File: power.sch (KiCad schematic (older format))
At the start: 42 parts, among them CN400 POWER_CONN, U108 74LS74A, U607 74LS08

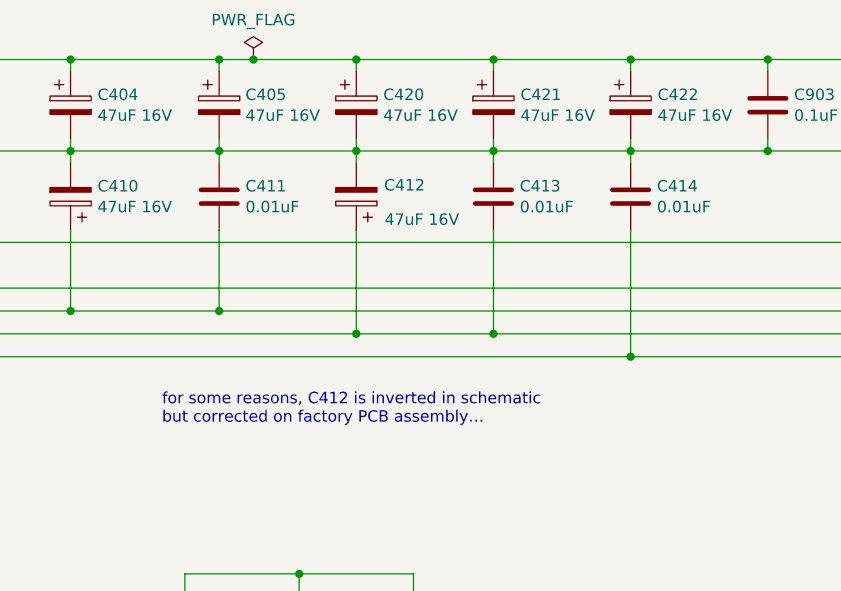
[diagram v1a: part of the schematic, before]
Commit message: Switch footprints for suitable modern replacements
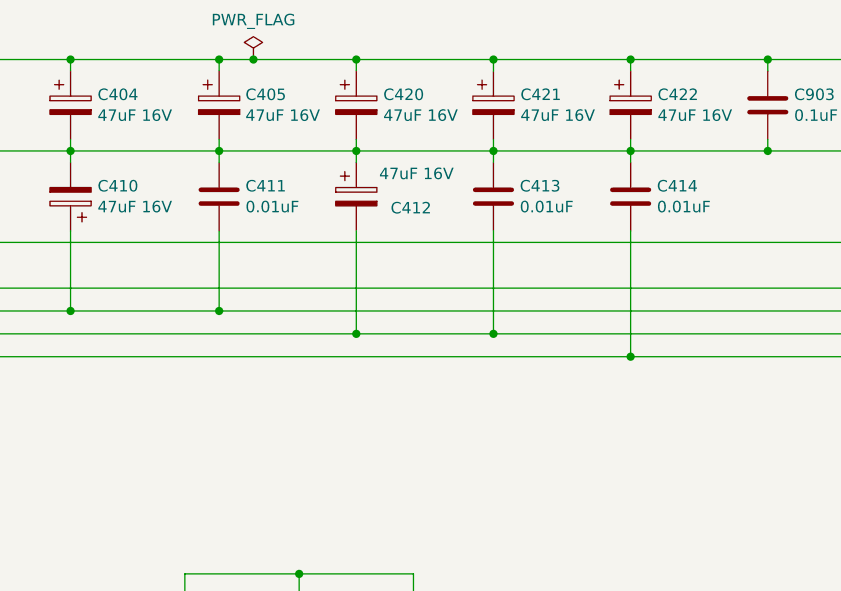
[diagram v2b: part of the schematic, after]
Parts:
- C401, C407, C409, C411, C413, C414, C903, C906, C910: footprint Capacitor_THT:C_Rect_L11.5mm_W2.0mm_P10.00mm_MKT -> Capacitor_THT:C_Rect_L11.5mm_W2.6mm_P10.00mm_MKT
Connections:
- net -5V: now also C412.2; no longer C412.1
- net GND: now also C412.1; no longer C412.2
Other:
- note removed: "for some reasons, C412 is inverted in schematic\nbut corrected on factory PCB assembly…"
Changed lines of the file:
@@
 F 0 "C401" H 2165 1746 50  0000 L CNN
 F 1 "0.01uF" H 2165 1655 50  0000 L CNN
-F 2 "Capacitor_THT:C_Rect_L11.5mm_W2.0mm_P10.00mm_MKT" H 2088 1550 50  0001 C CNN
+F 2 "Capacitor_THT:C_Rect_L11.5mm_W2.6mm_P10.00mm_MKT" H 2088 1550 50  0001 C CNN
 F 3 "~" H 2050 1700 50  0001 C CNN
 	1    2050 1700
@@
 F 0 "C407" H 2165 2146 50  0000 L CNN
 F 1 "0.01uF" H 2165 2055 50  0000 L CNN
-F 2 "Capacitor_THT:C_Rect_L11.5mm_W2.0mm_P10.00mm_MKT" H 2088 1950 50  0001 C CNN
+F 2 "Capacitor_THT:C_Rect_L11.5mm_W2.6mm_P10.00mm_MKT" H 2088 1950 50  0001 C CNN
 F 3 "~" H 2050 2100 50  0001 C CNN
 	1    2050 2100
-	1    0    0    -1
-$EndComp
-$Comp
-L Device:CP C408
-U 1 1 5DDDE124
-P 3050 2100
-F 0 "C408" H 3168 2146 50  0000 L CNN
-F 1 "47uF 16V" H 3168 2055 50  0000 L CNN
-F 2 "Capacitor_THT:CP_Radial_D8.0mm_P5.00mm" H 3088 1950 50  0001 C CNN
-F 3 "~" H 3050 2100 50  0001 C CNN
-	1    3050 2100
 	1    0    0    -1
 $EndComp
@@
 F 0 "C409" H 3815 2146 50  0000 L CNN
 F 1 "0.01uF" H 3815 2055 50  0000 L CNN
-F 2 "Capacitor_THT:C_Rect_L11.5mm_W2.0mm_P10.00mm_MKT" H 3738 1950 50  0001 C CNN
+F 2 "Capacitor_THT:C_Rect_L11.5mm_W2.6mm_P10.00mm_MKT" H 3738 1950 50  0001 C CNN
 F 3 "~" H 3700 2100 50  0001 C CNN
 	1    3700 2100
@@
 F 0 "C411" H 5265 2146 50  0000 L CNN
 F 1 "0.01uF" H 5265 2055 50  0000 L CNN
-F 2 "Capacitor_THT:C_Rect_L11.5mm_W2.0mm_P10.00mm_MKT" H 5188 1950 50  0001 C CNN
+F 2 "Capacitor_THT:C_Rect_L11.5mm_W2.6mm_P10.00mm_MKT" H 5188 1950 50  0001 C CNN
 F 3 "~" H 5150 2100 50  0001 C CNN
 	1    5150 2100
@@
 U 1 1 5DDDF78A
 P 5750 2100
-F 0 "C412" H 5450 2050 50  0000 L CNN
-F 1 "47uF 16V" H 5300 2200 50  0000 L CNN
+F 0 "C412" H 5900 2050 50  0000 L CNN
+F 1 "47uF 16V" H 5850 2200 50  0000 L CNN
 F 2 "Capacitor_THT:CP_Radial_D8.0mm_P5.00mm" H 5788 1950 50  0001 C CNN
 F 3 "~" H 5750 2100 50  0001 C CNN
 	1    5750 2100
-	-1   0    0    1
+	1    0    0    -1
 $EndComp
 $Comp
@@
 F 0 "C413" H 6465 2146 50  0000 L CNN
 F 1 "0.01uF" H 6465 2055 50  0000 L CNN
-F 2 "Capacitor_THT:C_Rect_L11.5mm_W2.0mm_P10.00mm_MKT" H 6388 1950 50  0001 C CNN
+F 2 "Capacitor_THT:C_Rect_L11.5mm_W2.6mm_P10.00mm_MKT" H 6388 1950 50  0001 C CNN
 F 3 "~" H 6350 2100 50  0001 C CNN
 	1    6350 2100
@@
 F 0 "C414" H 7065 2146 50  0000 L CNN
 F 1 "0.01uF" H 7065 2055 50  0000 L CNN
-F 2 "Capacitor_THT:C_Rect_L11.5mm_W2.0mm_P10.00mm_MKT" H 6988 1950 50  0001 C CNN
+F 2 "Capacitor_THT:C_Rect_L11.5mm_W2.6mm_P10.00mm_MKT" H 6988 1950 50  0001 C CNN
 F 3 "~" H 6950 2100 50  0001 C CNN
 	1    6950 2100
@@
 F 0 "C903" H 7665 1746 50  0000 L CNN
 F 1 "0.1uF" H 7665 1655 50  0000 L CNN
-F 2 "Capacitor_THT:C_Rect_L11.5mm_W2.0mm_P10.00mm_MKT" H 7588 1550 50  0001 C CNN
+F 2 "Capacitor_THT:C_Rect_L11.5mm_W2.6mm_P10.00mm_MKT" H 7588 1550 50  0001 C CNN
 F 3 "~" H 7550 1700 50  0001 C CNN
 	1    7550 1700
@@
 F 0 "C906" H 8115 1746 50  0000 L CNN
 F 1 "0.1uF" H 8115 1655 50  0000 L CNN
-F 2 "Capacitor_THT:C_Rect_L11.5mm_W2.0mm_P10.00mm_MKT" H 8038 1550 50  0001 C CNN
+F 2 "Capacitor_THT:C_Rect_L11.5mm_W2.6mm_P10.00mm_MKT" H 8038 1550 50  0001 C CNN
 F 3 "~" H 8000 1700 50  0001 C CNN
 	1    8000 1700
@@
 F 0 "C910" H 8565 1746 50  0000 L CNN
 F 1 "0.1uF" H 8565 1655 50  0000 L CNN
-F 2 "Capacitor_THT:C_Rect_L11.5mm_W2.0mm_P10.00mm_MKT" H 8488 1550 50  0001 C CNN
+F 2 "Capacitor_THT:C_Rect_L11.5mm_W2.6mm_P10.00mm_MKT" H 8488 1550 50  0001 C CNN
 F 3 "~" H 8450 1700 50  0001 C CNN
 	1    8450 1700
@@
 Wire Wire Line
 	6000 4350 6000 4300
-Text Notes 4900 3100 0    50   ~ 0
-for some reasons, C412 is inverted in schematic\nbut corrected on factory PCB assembly…
+$Comp
+L Device:CP C408
+U 1 1 5DDDE124
+P 3050 2100
+F 0 "C408" H 3168 2146 50  0000 L CNN
+F 1 "47uF 16V" H 3168 2055 50  0000 L CNN
+F 2 "Capacitor_THT:CP_Radial_D8.0mm_P5.00mm" H 3088 1950 50  0001 C CNN
+F 3 "~" H 3050 2100 50  0001 C CNN
+	1    3050 2100
+	1    0    0    -1
+$EndComp
 $EndSCHEMATC

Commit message: Some footprints updates; Add all Mouser references
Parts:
- C400: RefOrder (none) -> 667-ECA-1CM221B
- C401, C407, C409, C411, C413, C414: RefOrder (none) -> 581-SA105C103K
- C402, C403, C404, C405, C406, C408, C410, C412, C420, C421, C422: RefOrder (none) -> 667-ECA-1CM470B
- C903, C906, C910: RefOrder (none) -> 581-SA105C104KARC
- D400, D401: RefOrder (none) -> 750-1N4001-G
- H1, H10, H11, H12, H13, H14, H2, H3, H4, H5, H6, H7, H8, H9: DoNotPopulate (none) -> yes
- U108: RefOrder (none) -> 595-SN74LS74AN
- U607: RefOrder (none) -> 595-SN74LS08N
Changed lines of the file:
@@
 F 2 "Capacitor_THT:CP_Radial_D8.0mm_P5.00mm" H 1438 1550 50  0001 C CNN
 F 3 "~" H 1400 1700 50  0001 C CNN
+F 4 "667-ECA-1CM221B" H 1400 1700 50  0001 C CNN "RefOrder"
 	1    1400 1700
 	1    0    0    -1
@@
 F 2 "Capacitor_THT:C_Rect_L11.5mm_W2.6mm_P10.00mm_MKT" H 2088 1550 50  0001 C CNN
 F 3 "~" H 2050 1700 50  0001 C CNN
+F 4 "581-SA105C103K" H 2050 1700 50  0001 C CNN "RefOrder"
 	1    2050 1700
 	1    0    0    -1
@@
 F 2 "Capacitor_THT:CP_Radial_D8.0mm_P5.00mm" H 3088 1550 50  0001 C CNN
 F 3 "~" H 3050 1700 50  0001 C CNN
+F 4 "667-ECA-1CM470B" H 3050 1700 50  0001 C CNN "RefOrder"
 	1    3050 1700
 	1    0    0    -1
@@
 F 2 "Capacitor_THT:CP_Radial_D8.0mm_P5.00mm" H 3738 1550 50  0001 C CNN
 F 3 "~" H 3700 1700 50  0001 C CNN
+F 4 "667-ECA-1CM470B" H 3700 1700 50  0001 C CNN "RefOrder"
 	1    3700 1700
 	1    0    0    -1
@@
 F 2 "Capacitor_THT:CP_Radial_D8.0mm_P5.00mm" H 4538 1550 50  0001 C CNN
 F 3 "~" H 4500 1700 50  0001 C CNN
+F 4 "667-ECA-1CM470B" H 4500 1700 50  0001 C CNN "RefOrder"
 	1    4500 1700
 	1    0    0    -1
@@
 F 2 "Capacitor_THT:CP_Radial_D8.0mm_P5.00mm" H 5188 1550 50  0001 C CNN
 F 3 "~" H 5150 1700 50  0001 C CNN
+F 4 "667-ECA-1CM470B" H 5150 1700 50  0001 C CNN "RefOrder"
 	1    5150 1700
 	1    0    0    -1
@@
 F 2 "Capacitor_THT:CP_Radial_D8.0mm_P5.00mm" H 1438 1950 50  0001 C CNN
 F 3 "~" H 1400 2100 50  0001 C CNN
+F 4 "667-ECA-1CM470B" H 1400 2100 50  0001 C CNN "RefOrder"
 	1    1400 2100
 	-1   0    0    1
@@
 F 2 "Capacitor_THT:C_Rect_L11.5mm_W2.6mm_P10.00mm_MKT" H 2088 1950 50  0001 C CNN
 F 3 "~" H 2050 2100 50  0001 C CNN
+F 4 "581-SA105C103K" H 2050 2100 50  0001 C CNN "RefOrder"
 	1    2050 2100
 	1    0    0    -1
@@
 F 2 "Capacitor_THT:C_Rect_L11.5mm_W2.6mm_P10.00mm_MKT" H 3738 1950 50  0001 C CNN
 F 3 "~" H 3700 2100 50  0001 C CNN
+F 4 "581-SA105C103K" H 3700 2100 50  0001 C CNN "RefOrder"
 	1    3700 2100
 	1    0    0    -1
@@
 F 2 "Capacitor_THT:CP_Radial_D8.0mm_P5.00mm" H 4538 1950 50  0001 C CNN
 F 3 "~" H 4500 2100 50  0001 C CNN
+F 4 "667-ECA-1CM470B" H 4500 2100 50  0001 C CNN "RefOrder"
 	1    4500 2100
 	-1   0    0    1
@@
 F 2 "Capacitor_THT:C_Rect_L11.5mm_W2.6mm_P10.00mm_MKT" H 5188 1950 50  0001 C CNN
 F 3 "~" H 5150 2100 50  0001 C CNN
+F 4 "581-SA105C103K" H 5150 2100 50  0001 C CNN "RefOrder"
 	1    5150 2100
 	1    0    0    -1
@@
 F 2 "Capacitor_THT:CP_Radial_D8.0mm_P5.00mm" H 5788 1950 50  0001 C CNN
 F 3 "~" H 5750 2100 50  0001 C CNN
+F 4 "667-ECA-1CM470B" H 5750 2100 50  0001 C CNN "RefOrder"
 	1    5750 2100
 	1    0    0    -1
@@
 F 2 "Capacitor_THT:C_Rect_L11.5mm_W2.6mm_P10.00mm_MKT" H 6388 1950 50  0001 C CNN
 F 3 "~" H 6350 2100 50  0001 C CNN
+F 4 "581-SA105C103K" H 6350 2100 50  0001 C CNN "RefOrder"
 	1    6350 2100
 	1    0    0    -1
@@
 F 2 "Capacitor_THT:C_Rect_L11.5mm_W2.6mm_P10.00mm_MKT" H 6988 1950 50  0001 C CNN
 F 3 "~" H 6950 2100 50  0001 C CNN
+F 4 "581-SA105C103K" H 6950 2100 50  0001 C CNN "RefOrder"
 	1    6950 2100
 	1    0    0    -1
@@
 F 2 "Diode_THT:D_DO-41_SOD81_P10.16mm_Horizontal" H 9300 1975 50  0001 C CNN
 F 3 "http://www.vishay.com/docs/88503/1n4001.pdf" H 9300 2150 50  0001 C CNN
+F 4 "750-1N4001-G" H 9300 2150 50  0001 C CNN "RefOrder"
 	1    9300 2150
 	0    1    1    0
@@
 F 2 "Diode_THT:D_DO-41_SOD81_P10.16mm_Horizontal" H 10100 1975 50  0001 C CNN
 F 3 "http://www.vishay.com/docs/88503/1n4001.pdf" H 10100 2150 50  0001 C CNN
+F 4 "750-1N4001-G" H 10100 2150 50  0001 C CNN "RefOrder"
 	1    10100 2150
 	0    -1   -1   0
@@
 F 2 "Package_DIP:DIP-14_W7.62mm_Socket" H 8450 4700 50  0001 C CNN
 F 3 "http://www.ti.com/lit/ds/symlink/sn74ls74a.pdf" H 8450 4700 50  0001 C CNN
+F 4 "595-SN74LS74AN" H 8450 4700 50  0001 C CNN "RefOrder"
 	1    8450 4700
 	1    0    0    -1
@@
 F 2 "Package_DIP:DIP-14_W7.62mm_Socket" H 8450 5650 50  0001 C CNN
 F 3 "http://www.ti.com/lit/gpn/sn74LS08" H 8450 5650 50  0001 C CNN
+F 4 "595-SN74LS08N" H 8450 5650 50  0001 C CNN "RefOrder"
 	3    8450 5650
 	1    0    0    -1
@@
 F 2 "Capacitor_THT:CP_Radial_D8.0mm_P5.00mm" H 5788 1550 50  0001 C CNN
 F 3 "~" H 5750 1700 50  0001 C CNN
+F 4 "667-ECA-1CM470B" H 5750 1700 50  0001 C CNN "RefOrder"
 	1    5750 1700
 	1    0    0    -1
@@
 F 2 "Capacitor_THT:CP_Radial_D8.0mm_P5.00mm" H 6388 1550 50  0001 C CNN
 F 3 "~" H 6350 1700 50  0001 C CNN
+F 4 "667-ECA-1CM470B" H 6350 1700 50  0001 C CNN "RefOrder"
 	1    6350 1700
 	1    0    0    -1
@@
 F 2 "Capacitor_THT:CP_Radial_D8.0mm_P5.00mm" H 6988 1550 50  0001 C CNN
 F 3 "~" H 6950 1700 50  0001 C CNN
+F 4 "667-ECA-1CM470B" H 6950 1700 50  0001 C CNN "RefOrder"
 	1    6950 1700
 	1    0    0    -1
@@
 F 2 "Capacitor_THT:C_Rect_L11.5mm_W2.6mm_P10.00mm_MKT" H 7588 1550 50  0001 C CNN
 F 3 "~" H 7550 1700 50  0001 C CNN
+F 4 "581-SA105C104KARC" H 7550 1700 50  0001 C CNN "RefOrder"
 	1    7550 1700
 	1    0    0    -1
@@
 F 2 "Capacitor_THT:C_Rect_L11.5mm_W2.6mm_P10.00mm_MKT" H 8038 1550 50  0001 C CNN
 F 3 "~" H 8000 1700 50  0001 C CNN
+F 4 "581-SA105C104KARC" H 8000 1700 50  0001 C CNN "RefOrder"
 	1    8000 1700
 	1    0    0    -1
@@
 F 2 "Capacitor_THT:C_Rect_L11.5mm_W2.6mm_P10.00mm_MKT" H 8488 1550 50  0001 C CNN
 F 3 "~" H 8450 1700 50  0001 C CNN
+F 4 "581-SA105C104KARC" H 8450 1700 50  0001 C CNN "RefOrder"
 	1    8450 1700
 	1    0    0    -1
@@
 F 2 "MountingHole:MountingHole_4mm_Pad_Via" H 1500 3900 50  0001 C CNN
 F 3 "~" H 1500 3900 50  0001 C CNN
+F 4 "yes" H 1500 3900 50  0001 C CNN "DoNotPopulate"
 	1    1500 3900
 	0    -1   -1   0
@@
 F 2 "MountingHole:MountingHole_4mm_Pad_Via" H 1500 4400 50  0001 C CNN
 F 3 "~" H 1500 4400 50  0001 C CNN
+F 4 "yes" H 1500 4400 50  0001 C CNN "DoNotPopulate"
 	1    1500 4400
 	0    -1   -1   0
@@
 F 2 "MountingHole:MountingHole_4mm_Pad_Via" H 1500 4900 50  0001 C CNN
 F 3 "~" H 1500 4900 50  0001 C CNN
+F 4 "yes" H 1500 4900 50  0001 C CNN "DoNotPopulate"
 	1    1500 4900
 	0    -1   -1   0
@@
 F 2 "MountingHole:MountingHole_4mm_Pad_Via" H 1500 5400 50  0001 C CNN
 F 3 "~" H 1500 5400 50  0001 C CNN
+F 4 "yes" H 1500 5400 50  0001 C CNN "DoNotPopulate"
 	1    1500 5400
 	0    -1   -1   0
@@
 F 2 "MountingHole:MountingHole_4mm_Pad_Via" H 1500 5900 50  0001 C CNN
 F 3 "~" H 1500 5900 50  0001 C CNN
+F 4 "yes" H 1500 5900 50  0001 C CNN "DoNotPopulate"
 	1    1500 5900
 	0    -1   -1   0
@@
 F 2 "MountingHole:MountingHole_4mm_Pad_Via" H 2500 3900 50  0001 C CNN
 F 3 "~" H 2500 3900 50  0001 C CNN
+F 4 "yes" H 2500 3900 50  0001 C CNN "DoNotPopulate"
 	1    2500 3900
 	0    1    1    0
@@
 F 2 "MountingHole:MountingHole_4mm_Pad_Via" H 2500 4400 50  0001 C CNN
 F 3 "~" H 2500 4400 50  0001 C CNN
+F 4 "yes" H 2500 4400 50  0001 C CNN "DoNotPopulate"
 	1    2500 4400
 	0    1    1    0
@@
 F 2 "MountingHole:MountingHole_4mm_Pad_Via" H 2500 4900 50  0001 C CNN
 F 3 "~" H 2500 4900 50  0001 C CNN
+F 4 "yes" H 2500 4900 50  0001 C CNN "DoNotPopulate"
 	1    2500 4900
 	0    1    1    0
@@
 F 2 "MountingHole:MountingHole_4mm_Pad_Via" H 2500 5900 50  0001 C CNN
 F 3 "~" H 2500 5900 50  0001 C CNN
+F 4 "yes" H 2500 5900 50  0001 C CNN "DoNotPopulate"
 	1    2500 5900
 	0    1    1    0
@@
 F 2 "MountingHole:MountingHole_4mm_Pad_Via" H 2500 5400 50  0001 C CNN
 F 3 "~" H 2500 5400 50  0001 C CNN
+F 4 "yes" H 2500 5400 50  0001 C CNN "DoNotPopulate"
 	1    2500 5400
 	0    1    1    0
@@
 F 2 "MountingHole:MountingHole_4mm_Pad_Via" H 2500 4150 50  0001 C CNN
 F 3 "~" H 2500 4150 50  0001 C CNN
+F 4 "yes" H 2500 4150 50  0001 C CNN "DoNotPopulate"
 	1    2500 4150
 	0    1    1    0
@@
 F 2 "MountingHole:MountingHole_4mm_Pad_Via" H 2500 4650 50  0001 C CNN
 F 3 "~" H 2500 4650 50  0001 C CNN
+F 4 "yes" H 2500 4650 50  0001 C CNN "DoNotPopulate"
 	1    2500 4650
 	0    1    1    0
@@
 F 2 "MountingHole:MountingHole_4mm_Pad_Via" H 2500 5150 50  0001 C CNN
 F 3 "~" H 2500 5150 50  0001 C CNN
+F 4 "yes" H 2500 5150 50  0001 C CNN "DoNotPopulate"
 	1    2500 5150
 	0    1    1    0
@@
 F 2 "MountingHole:MountingHole_4mm_Pad_Via" H 2500 5650 50  0001 C CNN
 F 3 "~" H 2500 5650 50  0001 C CNN
+F 4 "yes" H 2500 5650 50  0001 C CNN "DoNotPopulate"
 	1    2500 5650
 	0    1    1    0
@@
 F 2 "Capacitor_THT:CP_Radial_D8.0mm_P5.00mm" H 3088 1950 50  0001 C CNN
 F 3 "~" H 3050 2100 50  0001 C CNN
+F 4 "667-ECA-1CM470B" H 3050 2100 50  0001 C CNN "RefOrder"
 	1    3050 2100
 	1    0    0    -1

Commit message: Got the components, reduce some footprints
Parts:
- C400: footprint Capacitor_THT:CP_Radial_D8.0mm_P5.00mm -> Capacitor_THT:CP_Radial_Tantal_D6.0mm_P5.00mm
- C402, C403, C404, C405, C406, C408, C410, C412, C420, C421, C422: footprint Capacitor_THT:CP_Radial_D8.0mm_P5.00mm -> Capacitor_THT:CP_Radial_Tantal_D5.5mm_P5.00mm
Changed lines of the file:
@@
 F 0 "C400" H 1518 1746 50  0000 L CNN
 F 1 "220uF 16V" H 1518 1655 50  0000 L CNN
-F 2 "Capacitor_THT:CP_Radial_D8.0mm_P5.00mm" H 1438 1550 50  0001 C CNN
+F 2 "Capacitor_THT:CP_Radial_Tantal_D6.0mm_P5.00mm" H 1438 1550 50  0001 C CNN
 F 3 "~" H 1400 1700 50  0001 C CNN
 F 4 "667-ECA-1CM221B" H 1400 1700 50  0001 C CNN "RefOrder"
@@
 F 0 "C402" H 3168 1746 50  0000 L CNN
 F 1 "47uF 16V" H 3168 1655 50  0000 L CNN
-F 2 "Capacitor_THT:CP_Radial_D8.0mm_P5.00mm" H 3088 1550 50  0001 C CNN
+F 2 "Capacitor_THT:CP_Radial_Tantal_D5.5mm_P5.00mm" H 3088 1550 50  0001 C CNN
 F 3 "~" H 3050 1700 50  0001 C CNN
 F 4 "667-ECA-1CM470B" H 3050 1700 50  0001 C CNN "RefOrder"
@@
 F 0 "C403" H 3815 1746 50  0000 L CNN
 F 1 "47uF 16V" H 3815 1655 50  0000 L CNN
-F 2 "Capacitor_THT:CP_Radial_D8.0mm_P5.00mm" H 3738 1550 50  0001 C CNN
+F 2 "Capacitor_THT:CP_Radial_Tantal_D5.5mm_P5.00mm" H 3738 1550 50  0001 C CNN
 F 3 "~" H 3700 1700 50  0001 C CNN
 F 4 "667-ECA-1CM470B" H 3700 1700 50  0001 C CNN "RefOrder"
@@
 F 0 "C404" H 4618 1746 50  0000 L CNN
 F 1 "47uF 16V" H 4618 1655 50  0000 L CNN
-F 2 "Capacitor_THT:CP_Radial_D8.0mm_P5.00mm" H 4538 1550 50  0001 C CNN
+F 2 "Capacitor_THT:CP_Radial_Tantal_D5.5mm_P5.00mm" H 4538 1550 50  0001 C CNN
 F 3 "~" H 4500 1700 50  0001 C CNN
 F 4 "667-ECA-1CM470B" H 4500 1700 50  0001 C CNN "RefOrder"
@@
 F 0 "C405" H 5265 1746 50  0000 L CNN
 F 1 "47uF 16V" H 5265 1655 50  0000 L CNN
-F 2 "Capacitor_THT:CP_Radial_D8.0mm_P5.00mm" H 5188 1550 50  0001 C CNN
+F 2 "Capacitor_THT:CP_Radial_Tantal_D5.5mm_P5.00mm" H 5188 1550 50  0001 C CNN
 F 3 "~" H 5150 1700 50  0001 C CNN
 F 4 "667-ECA-1CM470B" H 5150 1700 50  0001 C CNN "RefOrder"
@@
 F 0 "C406" H 1282 2054 50  0000 R CNN
 F 1 "47uF 16V" H 1282 2145 50  0000 R CNN
-F 2 "Capacitor_THT:CP_Radial_D8.0mm_P5.00mm" H 1438 1950 50  0001 C CNN
+F 2 "Capacitor_THT:CP_Radial_Tantal_D5.5mm_P5.00mm" H 1438 1950 50  0001 C CNN
 F 3 "~" H 1400 2100 50  0001 C CNN
 F 4 "667-ECA-1CM470B" H 1400 2100 50  0001 C CNN "RefOrder"
@@
 F 0 "C410" H 4382 2054 50  0000 R CNN
 F 1 "47uF 16V" H 4382 2145 50  0000 R CNN
-F 2 "Capacitor_THT:CP_Radial_D8.0mm_P5.00mm" H 4538 1950 50  0001 C CNN
+F 2 "Capacitor_THT:CP_Radial_Tantal_D5.5mm_P5.00mm" H 4538 1950 50  0001 C CNN
 F 3 "~" H 4500 2100 50  0001 C CNN
 F 4 "667-ECA-1CM470B" H 4500 2100 50  0001 C CNN "RefOrder"
@@
 F 0 "C412" H 5900 2050 50  0000 L CNN
 F 1 "47uF 16V" H 5850 2200 50  0000 L CNN
-F 2 "Capacitor_THT:CP_Radial_D8.0mm_P5.00mm" H 5788 1950 50  0001 C CNN
+F 2 "Capacitor_THT:CP_Radial_Tantal_D5.5mm_P5.00mm" H 5788 1950 50  0001 C CNN
 F 3 "~" H 5750 2100 50  0001 C CNN
 F 4 "667-ECA-1CM470B" H 5750 2100 50  0001 C CNN "RefOrder"
@@
 F 0 "C420" H 5868 1746 50  0000 L CNN
 F 1 "47uF 16V" H 5868 1655 50  0000 L CNN
-F 2 "Capacitor_THT:CP_Radial_D8.0mm_P5.00mm" H 5788 1550 50  0001 C CNN
+F 2 "Capacitor_THT:CP_Radial_Tantal_D5.5mm_P5.00mm" H 5788 1550 50  0001 C CNN
 F 3 "~" H 5750 1700 50  0001 C CNN
 F 4 "667-ECA-1CM470B" H 5750 1700 50  0001 C CNN "RefOrder"
@@
 F 0 "C421" H 6468 1746 50  0000 L CNN
 F 1 "47uF 16V" H 6468 1655 50  0000 L CNN
-F 2 "Capacitor_THT:CP_Radial_D8.0mm_P5.00mm" H 6388 1550 50  0001 C CNN
+F 2 "Capacitor_THT:CP_Radial_Tantal_D5.5mm_P5.00mm" H 6388 1550 50  0001 C CNN
 F 3 "~" H 6350 1700 50  0001 C CNN
 F 4 "667-ECA-1CM470B" H 6350 1700 50  0001 C CNN "RefOrder"
@@
 F 0 "C422" H 7068 1746 50  0000 L CNN
 F 1 "47uF 16V" H 7068 1655 50  0000 L CNN
-F 2 "Capacitor_THT:CP_Radial_D8.0mm_P5.00mm" H 6988 1550 50  0001 C CNN
+F 2 "Capacitor_THT:CP_Radial_Tantal_D5.5mm_P5.00mm" H 6988 1550 50  0001 C CNN
 F 3 "~" H 6950 1700 50  0001 C CNN
 F 4 "667-ECA-1CM470B" H 6950 1700 50  0001 C CNN "RefOrder"
@@
 F 0 "C408" H 3168 2146 50  0000 L CNN
 F 1 "47uF 16V" H 3168 2055 50  0000 L CNN
-F 2 "Capacitor_THT:CP_Radial_D8.0mm_P5.00mm" H 3088 1950 50  0001 C CNN
+F 2 "Capacitor_THT:CP_Radial_Tantal_D5.5mm_P5.00mm" H 3088 1950 50  0001 C CNN
 F 3 "~" H 3050 2100 50  0001 C CNN
 F 4 "667-ECA-1CM470B" H 3050 2100 50  0001 C CNN "RefOrder"
